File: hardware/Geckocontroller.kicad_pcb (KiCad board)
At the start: 2 copper layers, 114.3 x 96.5 mm, 115 parts, among them J101 AC Input, J11 RGB LED, J21 I²C (BME280), J31 DS18B20 I, J32 DS18B20 II, J40 FAN, J50 USB-C, J51 UART, J60 Load Cell Connector, J70 SPI / Addon Connector, J81 Dimmer, J91 Pump, J92 HeatBed, J93 HeatLamp, K81 AQG12212, K91 AQG12112, K92 AQG12112, K93 AQG12112, Q11 AO3400A, Q12 AO3400A, Q13 AO3400A, Q40 AO3400A, Q41 AO3401A, Q51 S8050, Q52 S8050, Q61 S8550, Q81 AO3400A, Q91 AO3400A, Q92 AO3400A, Q93 AO3400A, SW1 Boot, SW2 Reset, U1 ESP32-WROOM-32, U101 ACT4088, U2 CP2102, U61 HX711, U81 6N138

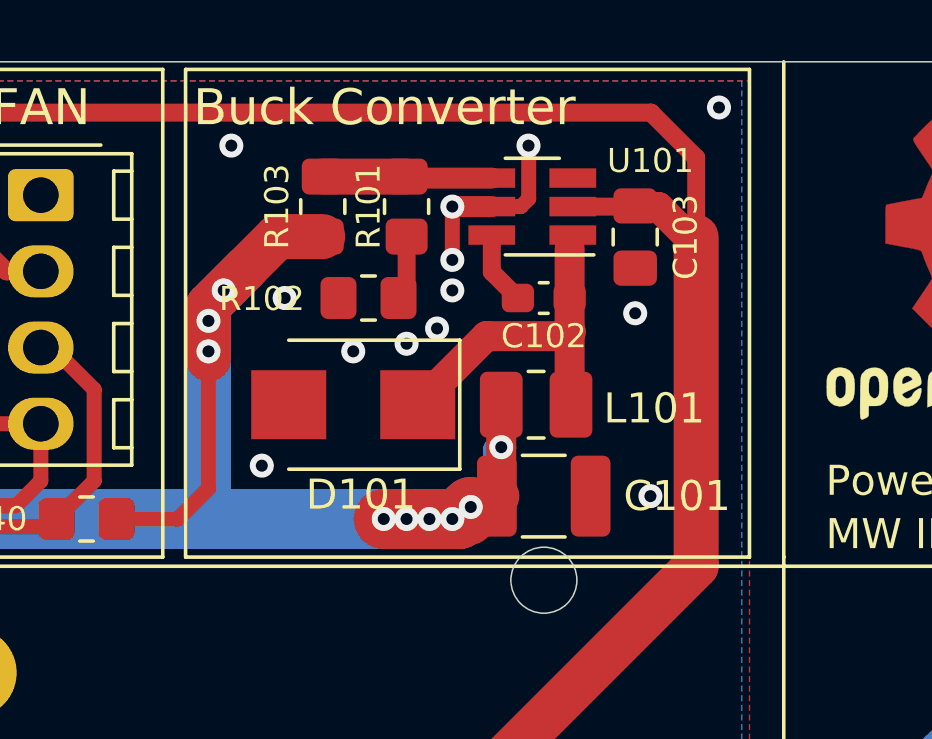
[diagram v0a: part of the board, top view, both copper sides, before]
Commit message: Controller Schema+PCB: Add Power-LED (Stand-by)
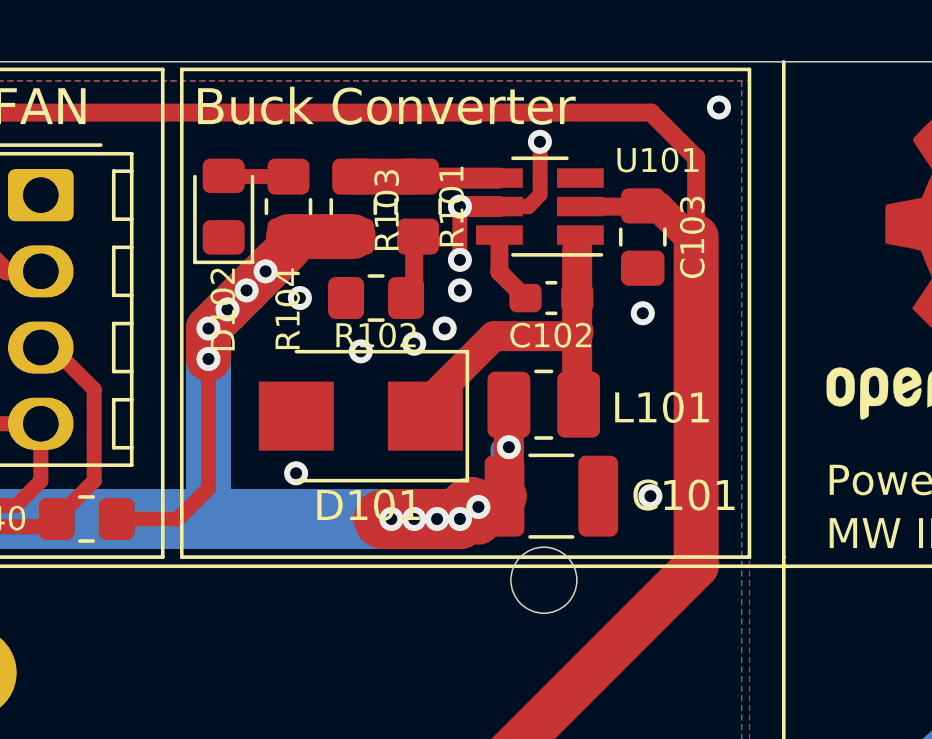
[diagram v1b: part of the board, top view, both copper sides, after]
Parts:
- added D102: LED, LED_SMD:LED_0805_2012Metric_Pad1.15x1.40mm_HandSolder, F.Cu at (70.9, 17.5)
- added R104: 470R, Resistor_SMD:R_0805_2012Metric_Pad1.20x1.40mm_HandSolder, F.Cu at (73.0, 17.5)
- moved R103 1.02 mm to (75.2, 17.5)
- moved D101 0.46 mm to (75.4, 24.5)
- moved R101 0.38 mm to (77.3, 17.5)
- moved C103 0.25 mm to (84.8, 18.5)
- moved L101 0.25 mm to (81.5, 24.1)
- moved R102 0.25 mm to (75.9, 20.6)
- moved C101 0.25 mm to (81.8, 27.2)
- moved C102 0.25 mm to (81.8, 20.6)
- moved U101 0.25 mm to (81.4, 17.5)
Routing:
- net Net-(D102-Pad2): track 0.00 -> 2.17 mm
- net +3V3: track 357.8 -> 359.0 mm, vias 14 -> 16
- net Net-(R101-Pad2): track 5.66 -> 4.89 mm
- net GND: vias 92 -> 91

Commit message: Controller PCB: Fix typo
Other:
- board text added: "HeatBed"
- board text removed: "HeadBed"

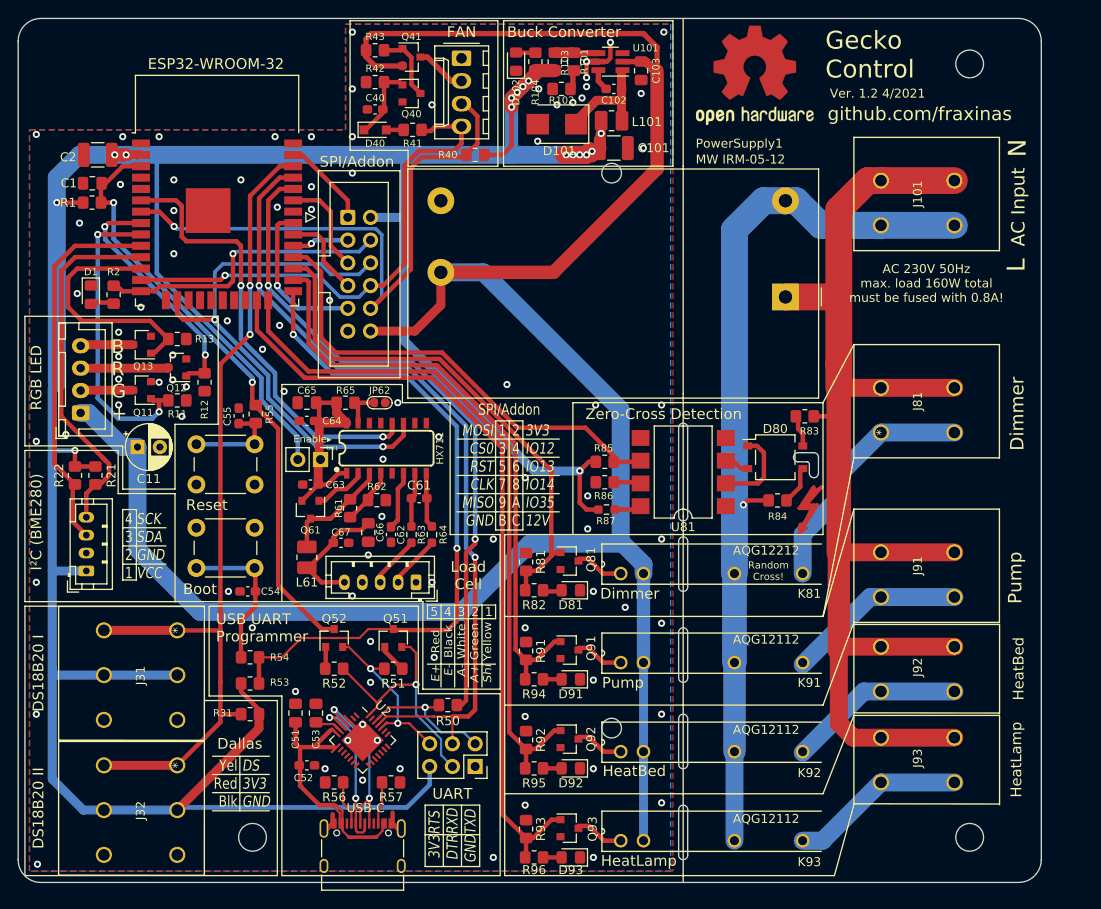
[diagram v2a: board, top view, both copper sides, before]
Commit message: Controller Hardware: Convert Project to KiCad 6
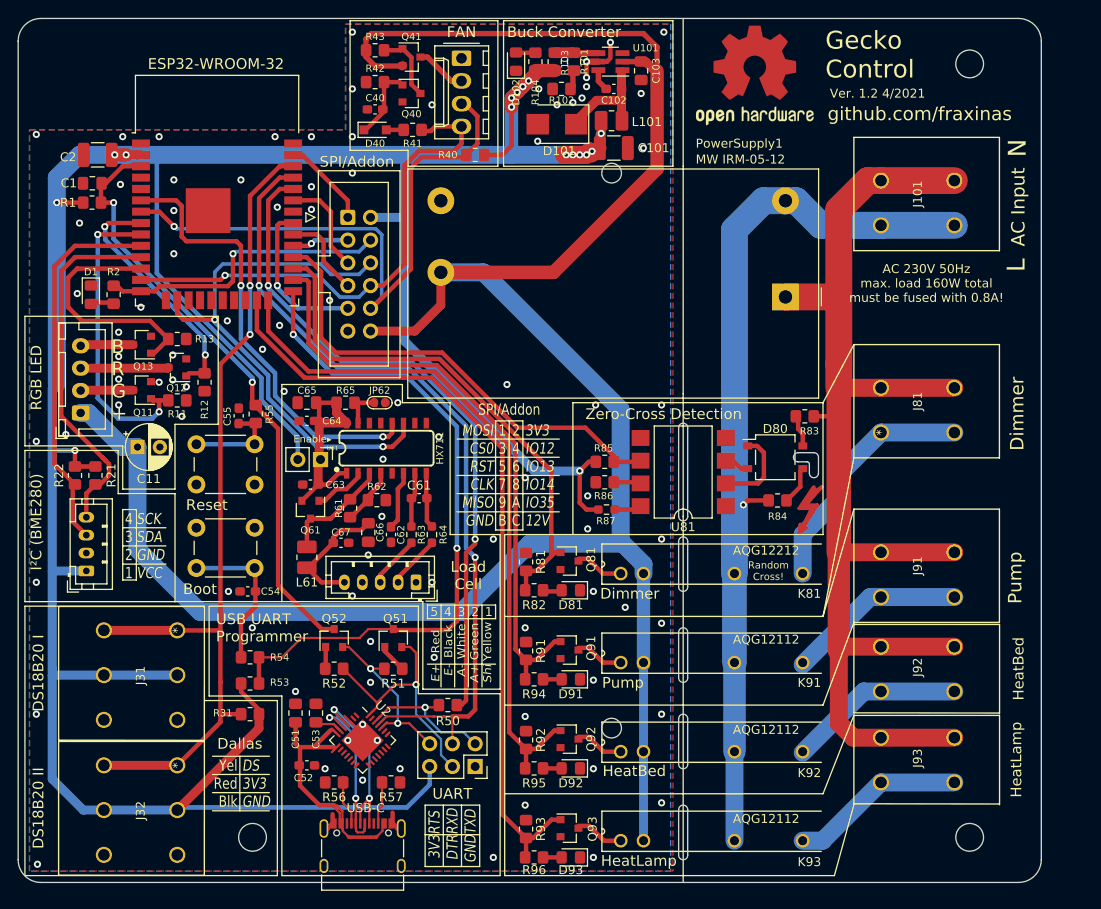
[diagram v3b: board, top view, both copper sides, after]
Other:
- net class Default removed
